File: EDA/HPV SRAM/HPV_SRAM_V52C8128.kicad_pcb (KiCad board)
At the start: 2 copper layers, 102.9 x 19.1 mm, 4 parts, among them J1 SIMM-68, J2 SIMM-68

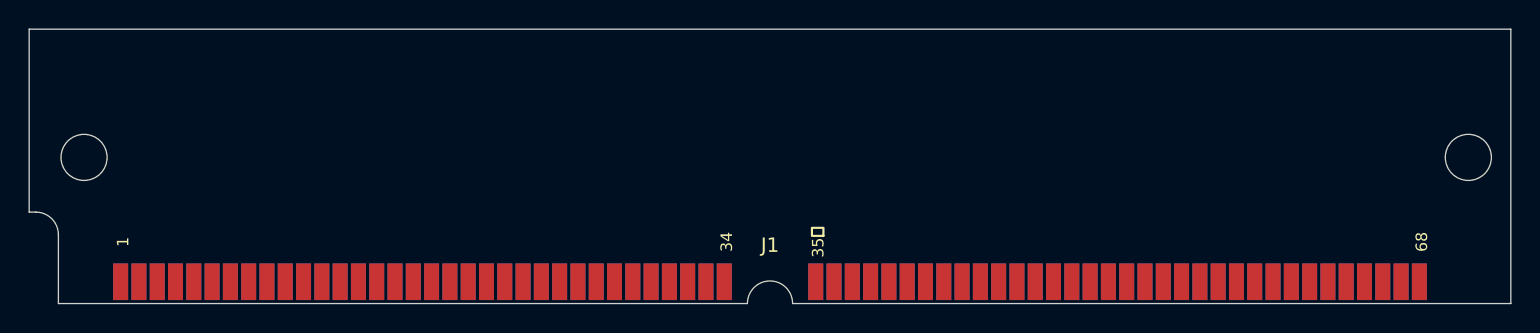
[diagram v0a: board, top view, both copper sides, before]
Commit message: HPV Riser Rev 1.2: Routing and PCB Edge fixes
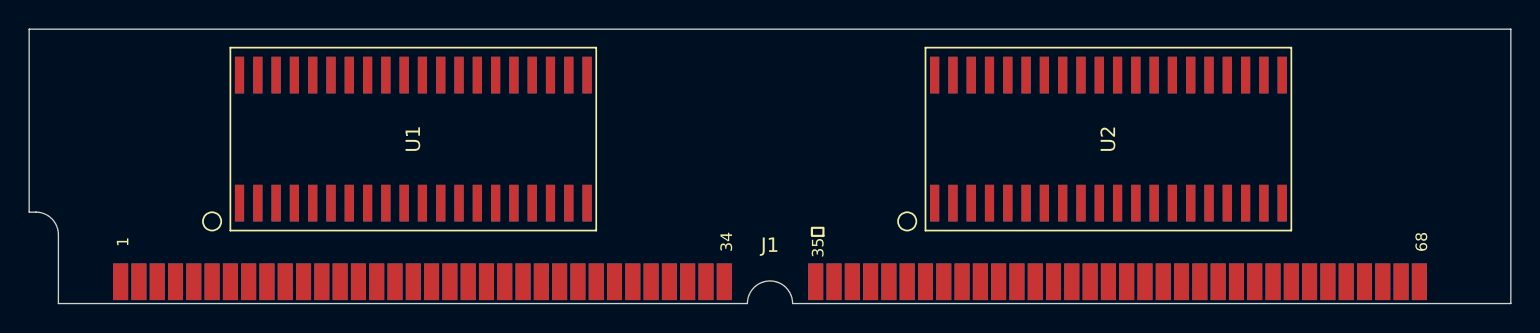
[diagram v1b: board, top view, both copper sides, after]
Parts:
- removed REF** (x2): MountingHole_3.2mm_M3_Pad, MountingHole:MountingHole_3.2mm_M3_Pad
- added U1: V52C8128, Connector_Apple:SOJ-40, F.Cu at (77.5, 58.4)
- added U2: V52C8128, Connector_Apple:SOJ-40, F.Cu at (125.7, 58.4)
- added U3: V52C8128, Connector_Apple:SOJ-40, B.Cu at (125.7, 58.4)
- added U4: V52C8128, Connector_Apple:SOJ-40, B.Cu at (77.5, 58.4)

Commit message: finished schema for V52C8128 256k VRAM stick
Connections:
- U1 pad 1: (no net) -> /SC
- U1 pad 14: (no net) -> /RAS
- U1 pad 31: (no net) -> /DQ4
- U1 pad 32: (no net) -> /DQ5
- U1 pad 33: (no net) -> /DQ6
- U1 pad 34: (no net) -> /DQ7
- U1 pad 36: (no net) -> /SDQ4
- U1 pad 37: (no net) -> /SDQ5
- U1 pad 38: (no net) -> /SDQ6
- U1 pad 39: (no net) -> /SDQ7
- U1 pad 7: (no net) -> /DQ0
- U1 pad 9: (no net) -> /DQ2
- U2 pad 1: (no net) -> /SC
- U3 pad 1: (no net) -> /SC
- U3 pad 10: (no net) -> /DQ11
- U3 pad 14: (no net) -> /RAS
- U3 pad 2: (no net) -> /SDQ8
- U3 pad 3: (no net) -> /SDQ9
- U3 pad 31: (no net) -> /DQ12
- U3 pad 32: (no net) -> /DQ13
- U3 pad 33: (no net) -> /DQ14
- U3 pad 34: (no net) -> /DQ15
- U3 pad 36: (no net) -> /SDQ12
- U3 pad 37: (no net) -> /SDQ13
- U3 pad 38: (no net) -> /SDQ14
- U3 pad 39: (no net) -> /SDQ15
- U3 pad 4: (no net) -> /SDQ10
- U3 pad 5: (no net) -> /SDQ11
- U3 pad 7: (no net) -> /DQ8
- U3 pad 8: (no net) -> /DQ9
- U4 pad 1: (no net) -> /SC
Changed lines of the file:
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@@
     (pad 40 connect rect (at 4.445 -12.065 90) (size 2.54 0.635) (layers F.Cu F.Mask)
       (net 2 GND))
-    (pad 39 connect rect (at 4.445 -10.795 90) (size 2.54 0.635) (layers F.Cu F.Mask))
-    (pad 38 connect rect (at 4.445 -9.525 90) (size 2.54 0.635) (layers F.Cu F.Mask))
-    (pad 37 connect rect (at 4.445 -8.255 90) (size 2.54 0.635) (layers F.Cu F.Mask))
-    (pad 36 connect rect (at 4.445 -6.985 90) (size 2.54 0.635) (layers F.Cu F.Mask))
+    (pad 39 connect rect (at 4.445 -10.795 90) (size 2.54 0.635) (layers F.Cu F.Mask)
+      (net 9 /SDQ7))
+    (pad 38 connect rect (at 4.445 -9.525 90) (size 2.54 0.635) (layers F.Cu F.Mask)
+      (net 8 /SDQ6))
+    (pad 37 connect rect (at 4.445 -8.255 90) (size 2.54 0.635) (layers F.Cu F.Mask)
+      (net 12 /SDQ5))
+    (pad 36 connect rect (at 4.445 -6.985 90) (size 2.54 0.635) (layers F.Cu F.Mask)
+      (net 13 /SDQ4))
     (pad 35 connect rect (at 4.445 -5.715 90) (size 2.54 0.635) (layers F.Cu F.Mask))
-    (pad 34 connect rect (at 4.445 -4.445 90) (size 2.54 0.635) (layers F.Cu F.Mask))
-    (pad 33 connect rect (at 4.445 -3.175 90) (size 2.54 0.635) (layers F.Cu F.Mask))
-    (pad 32 connect rect (at 4.445 -1.905 90) (size 2.54 0.635) (layers F.Cu F.Mask))
-    (pad 31 connect rect (at 4.445 -0.635 90) (size 2.54 0.635) (layers F.Cu F.Mask))
+    (pad 34 connect rect (at 4.445 -4.445 90) (size 2.54 0.635) (layers F.Cu F.Mask)
+      (net 7 /DQ7))
+    (pad 33 connect rect (at 4.445 -3.175 90) (size 2.54 0.635) (layers F.Cu F.Mask)
+      (net 6 /DQ6))
+    (pad 32 connect rect (at 4.445 -1.905 90) (size 2.54 0.635) (layers F.Cu F.Mask)
+      (net 10 /DQ5))
+    (pad 31 connect rect (at 4.445 -0.635 90) (size 2.54 0.635) (layers F.Cu F.Mask)
+      (net 11 /DQ4))
     (pad 30 connect rect (at 4.445 0.635 90) (size 2.54 0.635) (layers F.Cu F.Mask)
       (net 2 GND))
@@
     (pad 16 connect rect (at -4.445 6.985 90) (size 2.54 0.635) (layers F.Cu F.Mask))
     (pad 15 connect rect (at -4.445 5.715 90) (size 2.54 0.635) (layers F.Cu F.Mask))
-    (pad 14 connect rect (at -4.445 4.445 90) (size 2.54 0.635) (layers F.Cu F.Mask))
+    (pad 14 connect rect (at -4.445 4.445 90) (size 2.54 0.635) (layers F.Cu F.Mask)
+      (net 21 /RAS))
     (pad 13 connect rect (at -4.445 3.175 90) (size 2.54 0.635) (layers F.Cu F.Mask))
     (pad 12 connect rect (at -4.445 1.905 90) (size 2.54 0.635) (layers F.Cu F.Mask)
@@
     (pad 10 connect rect (at -4.445 -0.635 90) (size 2.54 0.635) (layers F.Cu F.Mask)
       (net 19 /DQ3))
-    (pad 9 connect rect (at -4.445 -1.905 90) (size 2.54 0.635) (layers F.Cu F.Mask))
+    (pad 9 connect rect (at -4.445 -1.905 90) (size 2.54 0.635) (layers F.Cu F.Mask)
+      (net 18 /DQ2))
     (pad 8 connect rect (at -4.445 -3.175 90) (size 2.54 0.635) (layers F.Cu F.Mask)
       (net 25 /DQ1))
-    (pad 7 connect rect (at -4.445 -4.445 90) (size 2.54 0.635) (layers F.Cu F.Mask))
+    (pad 7 connect rect (at -4.445 -4.445 90) (size 2.54 0.635) (layers F.Cu F.Mask)
+      (net 26 /DQ0))
     (pad 6 connect rect (at -4.445 -5.715 90) (size 2.54 0.635) (layers F.Cu F.Mask)
       (net 27 /DR-OE0))
@@
     (pad 2 connect rect (at -4.445 -10.795 90) (size 2.54 0.635) (layers F.Cu F.Mask)
       (net 29 /SDQ0))
-    (pad 1 connect rect (at -4.445 -12.065 90) (size 2.54 0.635) (layers F.Cu F.Mask))
+    (pad 1 connect rect (at -4.445 -12.065 90) (size 2.54 0.635) (layers F.Cu F.Mask)
+      (net 54 /SC))
   )
   (module Connector_Apple:SOJ-40 (layer F.Cu)
@@
     (pad 3 connect rect (at -4.445 -9.525 90) (size 2.54 0.635) (layers F.Cu F.Mask))
     (pad 2 connect rect (at -4.445 -10.795 90) (size 2.54 0.635) (layers F.Cu F.Mask))
-    (pad 1 connect rect (at -4.445 -12.065 90) (size 2.54 0.635) (layers F.Cu F.Mask))
+    (pad 1 connect rect (at -4.445 -12.065 90) (size 2.54 0.635) (layers F.Cu F.Mask)
+      (net 54 /SC))
   )
   (module Connector_Apple:SOJ-40 (layer B.Cu)
@@
     (fp_line (start 6.35 12.7) (end 6.35 -12.7) (layer B.SilkS) (width 0.12))
     (fp_line (start -6.35 12.7) (end 6.35 12.7) (layer B.SilkS) (width 0.12))
-    (pad 1 connect rect (at -4.445 12.065 90) (size 2.54 0.635) (layers B.Cu B.Mask))
-    (pad 2 connect rect (at -4.445 10.795 90) (size 2.54 0.635) (layers B.Cu B.Mask))
-    (pad 3 connect rect (at -4.445 9.525 90) (size 2.54 0.635) (layers B.Cu B.Mask))
-    (pad 4 connect rect (at -4.445 8.255 90) (size 2.54 0.635) (layers B.Cu B.Mask))
-    (pad 5 connect rect (at -4.445 6.985 90) (size 2.54 0.635) (layers B.Cu B.Mask))
+    (pad 1 connect rect (at -4.445 12.065 90) (size 2.54 0.635) (layers B.Cu B.Mask)
+      (net 54 /SC))
+    (pad 2 connect rect (at -4.445 10.795 90) (size 2.54 0.635) (layers B.Cu B.Mask)
+      (net 53 /SDQ8))
+    (pad 3 connect rect (at -4.445 9.525 90) (size 2.54 0.635) (layers B.Cu B.Mask)
+      (net 52 /SDQ9))
+    (pad 4 connect rect (at -4.445 8.255 90) (size 2.54 0.635) (layers B.Cu B.Mask)
+      (net 47 /SDQ10))
+    (pad 5 connect rect (at -4.445 6.985 90) (size 2.54 0.635) (layers B.Cu B.Mask)
+      (net 48 /SDQ11))
     (pad 6 connect rect (at -4.445 5.715 90) (size 2.54 0.635) (layers B.Cu B.Mask))
-    (pad 7 connect rect (at -4.445 4.445 90) (size 2.54 0.635) (layers B.Cu B.Mask))
-    (pad 8 connect rect (at -4.445 3.175 90) (size 2.54 0.635) (layers B.Cu B.Mask))
+    (pad 7 connect rect (at -4.445 4.445 90) (size 2.54 0.635) (layers B.Cu B.Mask)
+      (net 50 /DQ8))
+    (pad 8 connect rect (at -4.445 3.175 90) (size 2.54 0.635) (layers B.Cu B.Mask)
+      (net 49 /DQ9))
     (pad 9 connect rect (at -4.445 1.905 90) (size 2.54 0.635) (layers B.Cu B.Mask))
-    (pad 10 connect rect (at -4.445 0.635 90) (size 2.54 0.635) (layers B.Cu B.Mask))
+    (pad 10 connect rect (at -4.445 0.635 90) (size 2.54 0.635) (layers B.Cu B.Mask)
+      (net 44 /DQ11))
     (pad 11 connect rect (at -4.445 -0.635 90) (size 2.54 0.635) (layers B.Cu B.Mask)
       (net 1 +5V))
     (pad 12 connect rect (at -4.445 -1.905 90) (size 2.54 0.635) (layers B.Cu B.Mask))
     (pad 13 connect rect (at -4.445 -3.175 90) (size 2.54 0.635) (layers B.Cu B.Mask))
-    (pad 14 connect rect (at -4.445 -4.445 90) (size 2.54 0.635) (layers B.Cu B.Mask))
+    (pad 14 connect rect (at -4.445 -4.445 90) (size 2.54 0.635) (layers B.Cu B.Mask)
+      (net 21 /RAS))
     (pad 15 connect rect (at -4.445 -5.715 90) (size 2.54 0.635) (layers B.Cu B.Mask))
     (pad 16 connect rect (at -4.445 -6.985 90) (size 2.54 0.635) (layers B.Cu B.Mask))
@@
     (pad 30 connect rect (at 4.445 -0.635 90) (size 2.54 0.635) (layers B.Cu B.Mask)
       (net 2 GND))
-    (pad 31 connect rect (at 4.445 0.635 90) (size 2.54 0.635) (layers B.Cu B.Mask))
-    (pad 32 connect rect (at 4.445 1.905 90) (size 2.54 0.635) (layers B.Cu B.Mask))
-    (pad 33 connect rect (at 4.445 3.175 90) (size 2.54 0.635) (layers B.Cu B.Mask))
-    (pad 34 connect rect (at 4.445 4.445 90) (size 2.54 0.635) (layers B.Cu B.Mask))
+    (pad 31 connect rect (at 4.445 0.635 90) (size 2.54 0.635) (layers B.Cu B.Mask)
+      (net 37 /DQ12))
+    (pad 32 connect rect (at 4.445 1.905 90) (size 2.54 0.635) (layers B.Cu B.Mask)
+      (net 36 /DQ13))
+    (pad 33 connect rect (at 4.445 3.175 90) (size 2.54 0.635) (layers B.Cu B.Mask)
+      (net 32 /DQ14))
+    (pad 34 connect rect (at 4.445 4.445 90) (size 2.54 0.635) (layers B.Cu B.Mask)
+      (net 33 /DQ15))
     (pad 35 connect rect (at 4.445 5.715 90) (size 2.54 0.635) (layers B.Cu B.Mask))
-    (pad 36 connect rect (at 4.445 6.985 90) (size 2.54 0.635) (layers B.Cu B.Mask))
-    (pad 37 connect rect (at 4.445 8.255 90) (size 2.54 0.635) (layers B.Cu B.Mask))
-    (pad 38 connect rect (at 4.445 9.525 90) (size 2.54 0.635) (layers B.Cu B.Mask))
-    (pad 39 connect rect (at 4.445 10.795 90) (size 2.54 0.635) (layers B.Cu B.Mask))
+    (pad 36 connect rect (at 4.445 6.985 90) (size 2.54 0.635) (layers B.Cu B.Mask)
+      (net 39 /SDQ12))
+    (pad 37 connect rect (at 4.445 8.255 90) (size 2.54 0.635) (layers B.Cu B.Mask)
+      (net 38 /SDQ13))
+    (pad 38 connect rect (at 4.445 9.525 90) (size 2.54 0.635) (layers B.Cu B.Mask)
+      (net 34 /SDQ14))
+    (pad 39 connect rect (at 4.445 10.795 90) (size 2.54 0.635) (layers B.Cu B.Mask)
+      (net 35 /SDQ15))
     (pad 40 connect rect (at 4.445 12.065 90) (size 2.54 0.635) (layers B.Cu B.Mask)
       (net 2 GND))
@@
     (fp_line (start 6.35 12.7) (end 6.35 -12.7) (layer B.SilkS) (width 0.12))
     (fp_line (start -6.35 12.7) (end 6.35 12.7) (layer B.SilkS) (width 0.12))
-    (pad 1 connect rect (at -4.445 12.065 90) (size 2.54 0.635) (layers B.Cu B.Mask))
+    (pad 1 connect rect (at -4.445 12.065 90) (size 2.54 0.635) (layers B.Cu B.Mask)
+      (net 54 /SC))
     (pad 2 connect rect (at -4.445 10.795 90) (size 2.54 0.635) (layers B.Cu B.Mask))
     (pad 3 connect rect (at -4.445 9.525 90) (size 2.54 0.635) (layers B.Cu B.Mask))
